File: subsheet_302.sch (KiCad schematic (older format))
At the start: 32 parts, among them J302 Internal FDD Power, J303 Internal FDD Port, J304 DIN-14S — External FDD Port, U301 WD1772_FLOPPY_DISK_CONTROLLER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, U305 7406_PHY

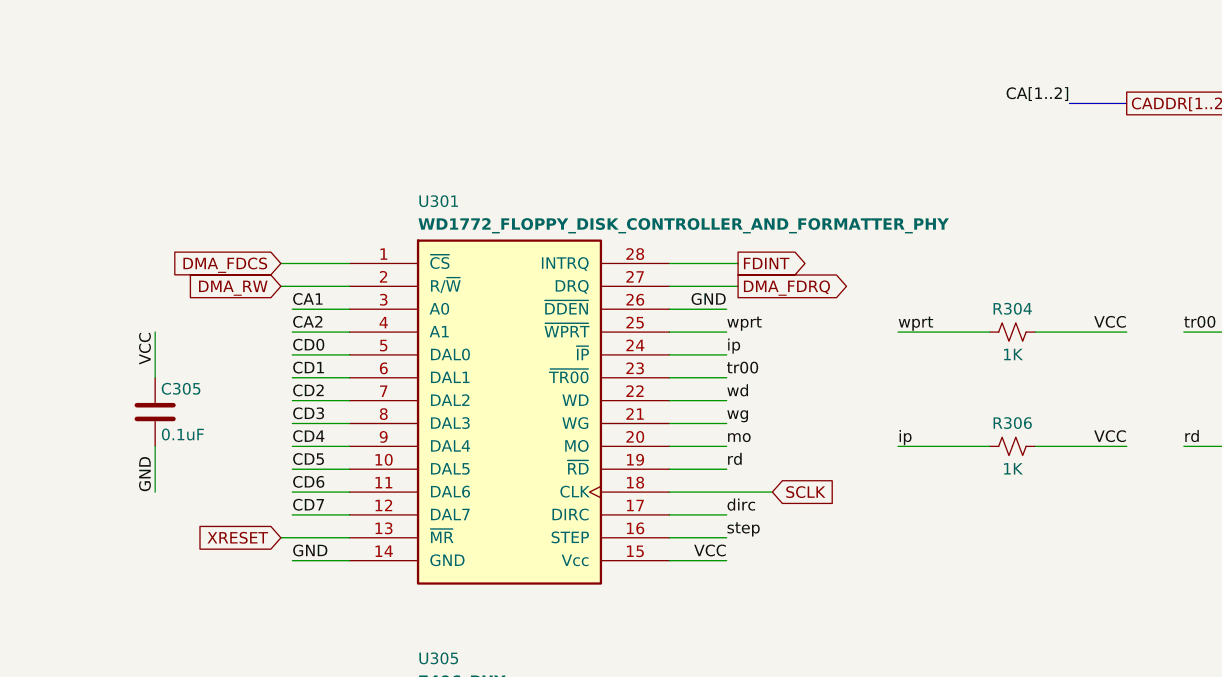
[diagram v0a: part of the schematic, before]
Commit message: [Schematics] Reference to the WD1772 databus pull-up fix
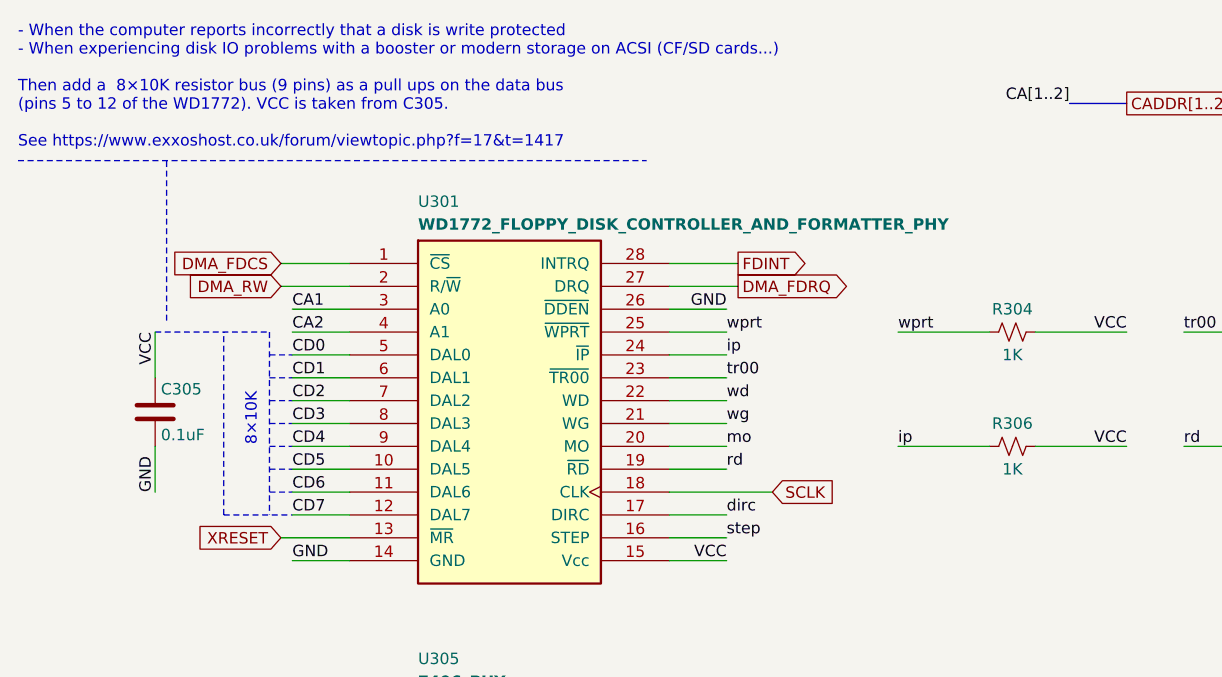
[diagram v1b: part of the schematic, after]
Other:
- note added: "- When the computer reports incorrectly that a disk is write protected\n- When experiencing disk IO problems with a booster or modern storage on ACSI (CF/SD cards...)\n\nThen add a 8×10K resistor bus (9 pins) as a pull ups on the data bus \n(pins 5 to 12 of the WD1772). VCC is taken from C305.\n\nSee https://www.exxoshost.co.uk/forum/viewtopic.php?f=17&t=1417"
- note added: "8×10K"
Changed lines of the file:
@@
 Wire Wire Line
 	6500 9100 6500 8900
+Text Notes 650  1200 0    50   ~ 0
+- When the computer reports incorrectly that a disk is write protected\n- When experiencing disk IO problems with a booster or modern storage on ACSI (CF/SD cards...)\n\nThen add a  8×10K resistor bus (9 pins) as a pull ups on the data bus \n(pins 5 to 12 of the WD1772). VCC is taken from C305.\n\nSee https://www.exxoshost.co.uk/forum/viewtopic.php?f=17&t=1417
+Wire Notes Line
+	1750 2000 1750 2800
+Wire Notes Line
+	1550 2800 1550 2000
+Wire Notes Line
+	1250 2000 1750 2000
+Wire Notes Line
+	1750 2100 1850 2100
+Wire Notes Line
+	1750 2200 1850 2200
+Wire Notes Line
+	1750 2300 1850 2300
+Wire Notes Line
+	1750 2400 1850 2400
+Wire Notes Line
+	1750 2500 1850 2500
+Wire Notes Line
+	1750 2600 1850 2600
+Wire Notes Line
+	1750 2700 1850 2700
+Wire Notes Line
+	1550 2800 1850 2800
+Text Notes 1700 2500 1    50   ~ 0
+8×10K
+Wire Notes Line
+	650  1250 3400 1250
+Wire Notes Line
+	1300 1950 1300 1250
 $EndSCHEMATC

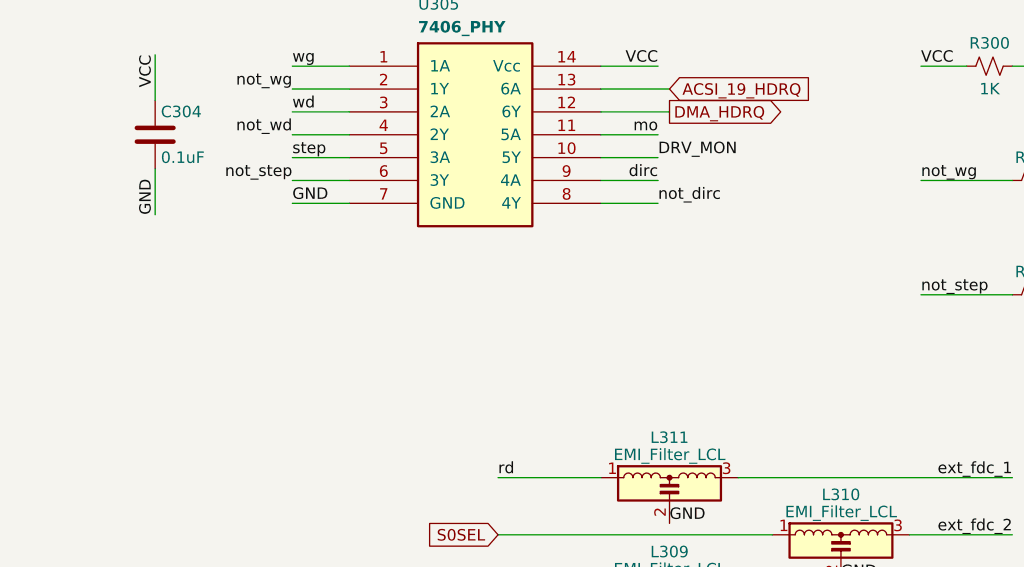
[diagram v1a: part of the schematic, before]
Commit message: [Schematics] Reference to the LS06 pull-up fix for the floppy drive
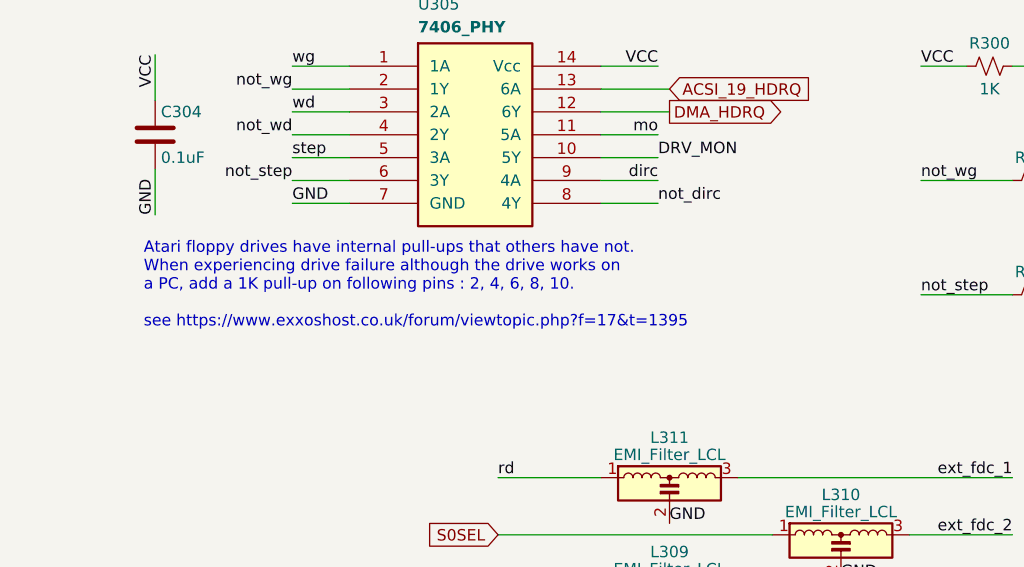
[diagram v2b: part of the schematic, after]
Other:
- note added: "Atari floppy drives have internal pull-ups that others have not.\nWhen experiencing drive failure although the drive works on\na PC, add a 1K pull-up on following pins : 2, 4, 6, 8, 10.\n\nsee https://www.exxoshost.co.uk/forum/viewtopic.php?f=17&t=1395"
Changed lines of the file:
@@
 Wire Notes Line
 	1300 1950 1300 1250
+Text Notes 1200 4850 0    50   ~ 0
+Atari floppy drives have internal pull-ups that others have not.\nWhen experiencing drive failure although the drive works on\na PC, add a 1K pull-up on following pins : 2, 4, 6, 8, 10.\n\nsee https://www.exxoshost.co.uk/forum/viewtopic.php?f=17&t=1395
 $EndSCHEMATC

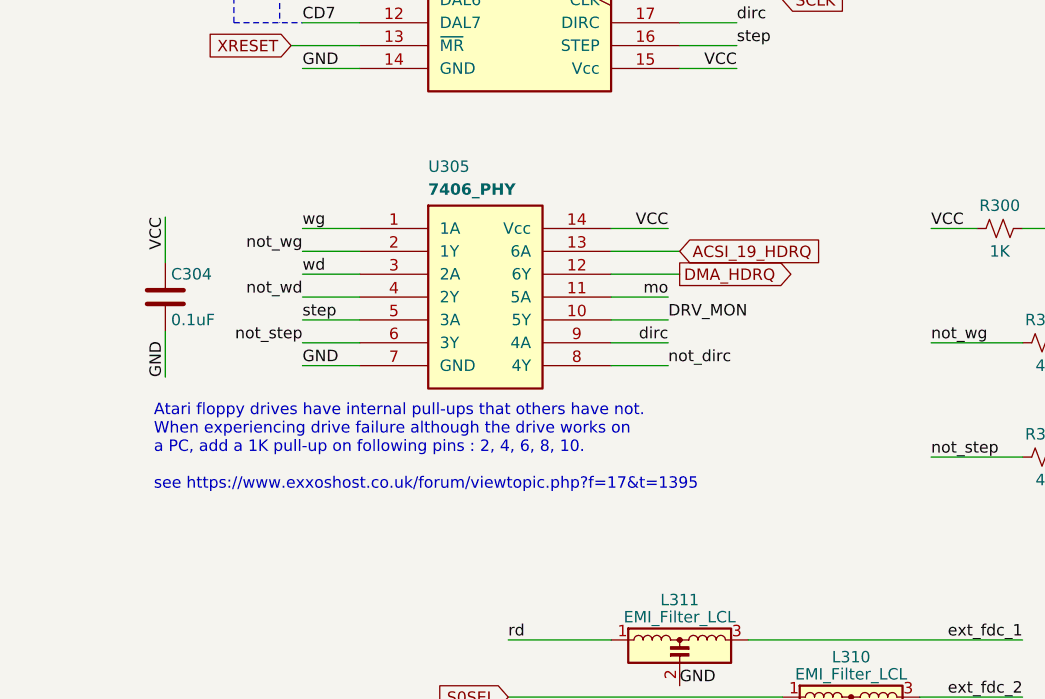
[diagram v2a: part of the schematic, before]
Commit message: [Schematics] graphical details for the pull-ups of drive signals fix
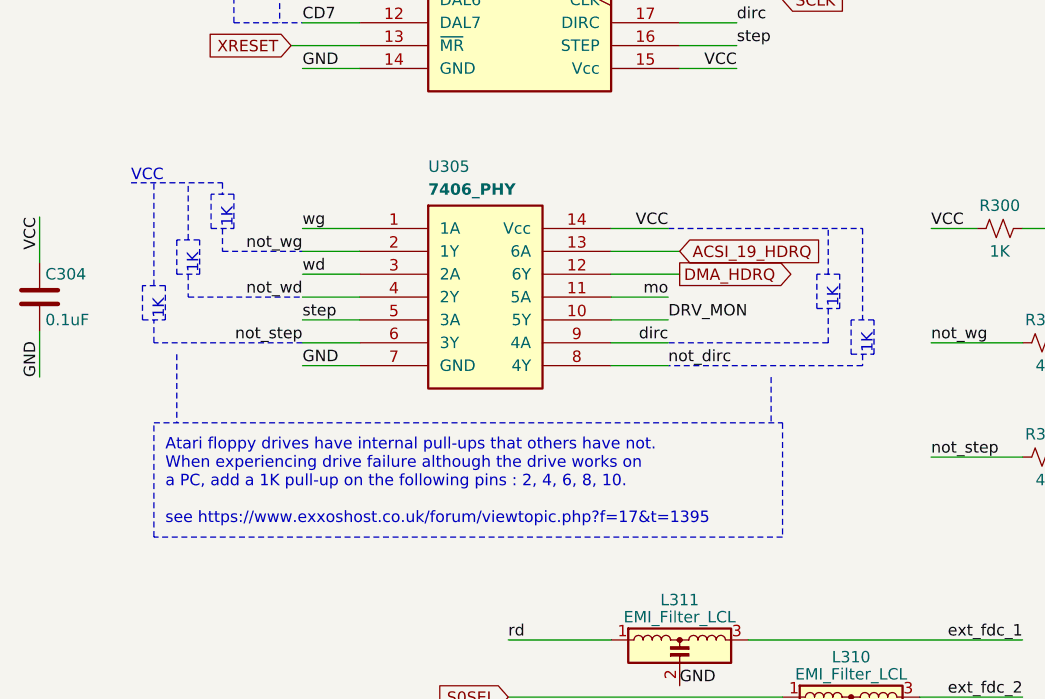
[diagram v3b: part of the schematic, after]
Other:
- note added: "1K"
- note added: "Atari floppy drives have internal pull-ups that others have not.\nWhen experiencing drive failure although the drive works on\na PC, add a 1K pull-up on the following pins : 2, 4, 6, 8, 10.\n\nsee https://www.exxoshost.co.uk/forum/viewtopic.php?f=17&t=1395"
- note added: "VCC"
- note removed: "Atari floppy drives have internal pull-ups that others have not.\nWhen experiencing drive failure although the drive works on\na PC, add a 1K pull-up on following pins : 2, 4, 6, 8, 10.\n\nsee https://www.exxoshost.co.uk/forum/viewtopic.php?f=17&t=1395"
- moved on the sheet: C304
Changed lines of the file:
@@
 L Device:C C?
 U 1 1 60ADC6E0
-P 1250 4000
+P 700 4000
 AR Path="/60786F27/6078774E/60ADC6E0" Ref="C?"  Part="1"
 AR Path="/60786F27/607875AF/60ADC6E0" Ref="C?"  Part="1"
@@
 AR Path="/60A73CDE/60ADC6E0" Ref="C?"  Part="1"
 AR Path="/60AD8617/60ADC6E0" Ref="C304"  Part="1"
-F 0 "C304" H 1275 4100 50  0000 L CNN
-F 1 "0.1uF" H 1275 3900 50  0000 L CNN
-F 2 "commons_passives_THT:Passive_THT_capacitor_mlcc_W2.54mm_L7.62mm" H 1288 3850 50  0001 C CNN
-F 3 "~" H 1250 4000 50  0001 C CNN
-	1    1250 4000
-	1    0    0    -1
-$EndComp
-Text Label 1250 4350 1    50   ~ 0
-GND
-Text Label 1250 3650 3    50   ~ 0
+F 0 "C304" H 725 4100 50  0000 L CNN
+F 1 "0.1uF" H 725 3900 50  0000 L CNN
+F 2 "commons_passives_THT:Passive_THT_capacitor_mlcc_W2.54mm_L7.62mm" H 738 3850 50  0001 C CNN
+F 3 "~" H 700 4000 50  0001 C CNN
+	1    700  4000
+	1    0    0    -1
+$EndComp
+Text Label 700  4350 1    50   ~ 0
+GND
+Text Label 700  3650 3    50   ~ 0
 VCC
 Wire Wire Line
-	1250 3650 1250 3850
-Wire Wire Line
-	1250 4150 1250 4350
+	700  3650 700  3850
+Wire Wire Line
+	700  4150 700  4350
 $Comp
 L Device:R_Small_US R?
@@
 Wire Notes Line
 	1300 1950 1300 1250
-Text Notes 1200 4850 0    50   ~ 0
-Atari floppy drives have internal pull-ups that others have not.\nWhen experiencing drive failure although the drive works on\na PC, add a 1K pull-up on following pins : 2, 4, 6, 8, 10.\n\nsee https://www.exxoshost.co.uk/forum/viewtopic.php?f=17&t=1395
+Text Notes 1250 5000 0    50   ~ 0
+Atari floppy drives have internal pull-ups that others have not.\nWhen experiencing drive failure although the drive works on\na PC, add a 1K pull-up on the following pins : 2, 4, 6, 8, 10.\n\nsee https://www.exxoshost.co.uk/forum/viewtopic.php?f=17&t=1395
+Wire Notes Line
+	1550 3550 1450 3550
+Wire Notes Line
+	1450 3550 1450 3700
+Wire Notes Line
+	1450 3700 1550 3700
+Wire Notes Line
+	1550 3700 1550 3550
+Text Notes 1550 3700 1    50   ~ 0
+1K
+Wire Notes Line
+	1400 3750 1300 3750
+Wire Notes Line
+	1300 3750 1300 3900
+Wire Notes Line
+	1300 3900 1400 3900
+Wire Notes Line
+	1400 3900 1400 3750
+Text Notes 1400 3900 1    50   ~ 0
+1K
+Wire Notes Line
+	1250 3950 1150 3950
+Wire Notes Line
+	1150 3950 1150 4100
+Wire Notes Line
+	1150 4100 1250 4100
+Wire Notes Line
+	1250 4100 1250 3950
+Text Notes 1250 4100 1    50   ~ 0
+1K
+Wire Notes Line
+	1850 4200 1200 4200
+Wire Notes Line
+	1200 4200 1200 4100
+Wire Notes Line
+	1350 3900 1350 4000
+Wire Notes Line
+	1350 4000 1850 4000
+Wire Notes Line
+	1500 3700 1500 3800
+Wire Notes Line
+	1500 3800 1850 3800
+Text Notes 1100 3500 0    50   ~ 0
+VCC
+Wire Notes Line
+	1100 3500 1500 3500
+Wire Notes Line
+	1500 3500 1500 3550
+Wire Notes Line
+	1350 3750 1350 3500
+Wire Notes Line
+	1200 3950 1200 3500
+Wire Notes Line
+	4200 3900 4100 3900
+Wire Notes Line
+	4100 3900 4100 4050
+Wire Notes Line
+	4100 4050 4200 4050
+Wire Notes Line
+	4200 4050 4200 3900
+Text Notes 4200 4050 1    50   ~ 0
+1K
+Wire Notes Line
+	4350 4100 4250 4100
+Wire Notes Line
+	4250 4100 4250 4250
+Wire Notes Line
+	4250 4250 4350 4250
+Wire Notes Line
+	4350 4250 4350 4100
+Text Notes 4350 4250 1    50   ~ 0
+1K
+Wire Notes Line
+	3450 3700 4300 3700
+Wire Notes Line
+	4300 3700 4300 4100
+Wire Notes Line
+	4300 4250 4300 4300
+Wire Notes Line
+	4300 4300 3450 4300
+Wire Notes Line
+	4150 4050 4150 4200
+Wire Notes Line
+	4150 4200 3450 4200
+Wire Notes Line
+	4150 3900 4150 3700
+Wire Notes Line
+	1200 4550 3950 4550
+Wire Notes Line
+	3950 4550 3950 5050
+Wire Notes Line
+	3950 5050 1200 5050
+Wire Notes Line
+	1200 5050 1200 4550
+Wire Notes Line
+	1300 4250 1300 4550
+Wire Notes Line
+	3900 4350 3900 4550
 $EndSCHEMATC

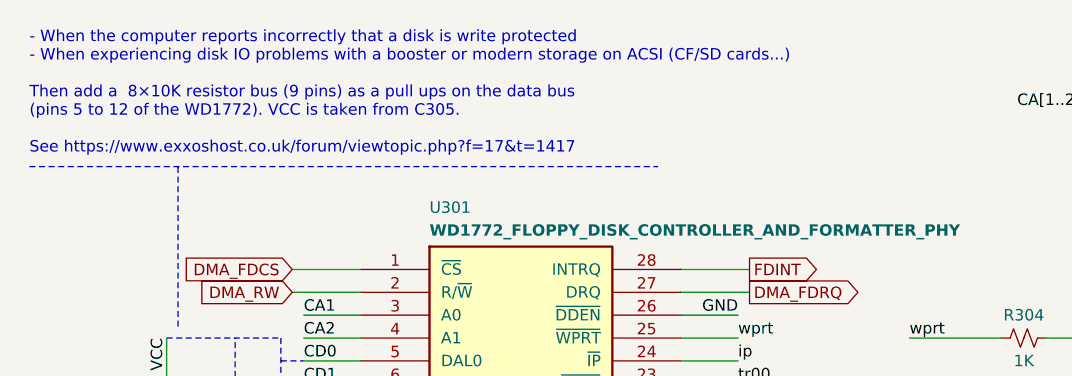
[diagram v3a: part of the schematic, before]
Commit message: Added a note about the presence of comment referencing some hardware fixes
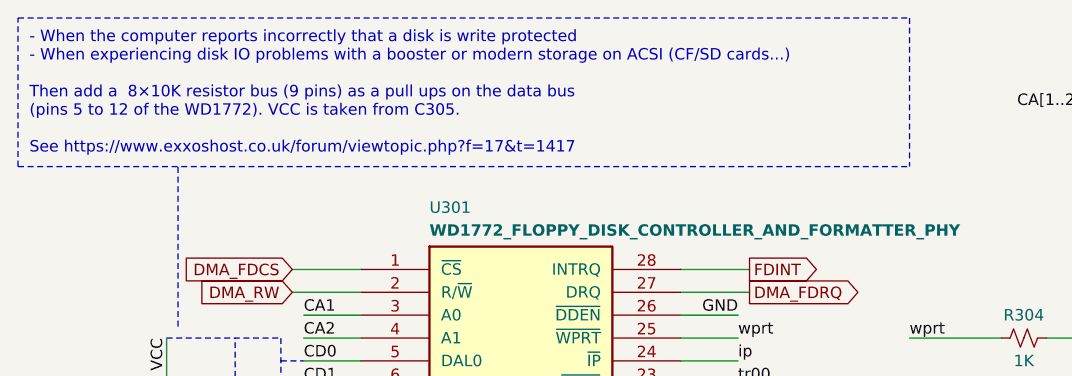
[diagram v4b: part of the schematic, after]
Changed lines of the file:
@@
 8×10K
-Wire Notes Line
-	650  1250 3400 1250
 Wire Notes Line
 	1300 1950 1300 1250
@@
 Wire Notes Line
 	3900 4350 3900 4550
+Wire Notes Line
+	600  1250 600  600
+Wire Notes Line
+	600  600  4500 600
+Wire Notes Line
+	4500 600  4500 1250
+Wire Notes Line
+	600  1250 4500 1250
 $EndSCHEMATC
